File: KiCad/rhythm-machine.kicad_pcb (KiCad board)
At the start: 4 copper layers, 76.2 x 69.8 mm, 23 parts, among them J1 MicroSDModule, J10 Fader, J11 LCD_I2C, J2 AudioAmpModule, J3 Button_LeftRed, J4 Button_LeftGreen, J5 Button_LeftBlue, J6 Button_RightRed, J7 Button_RightGreen, J8 Button_RightBlue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

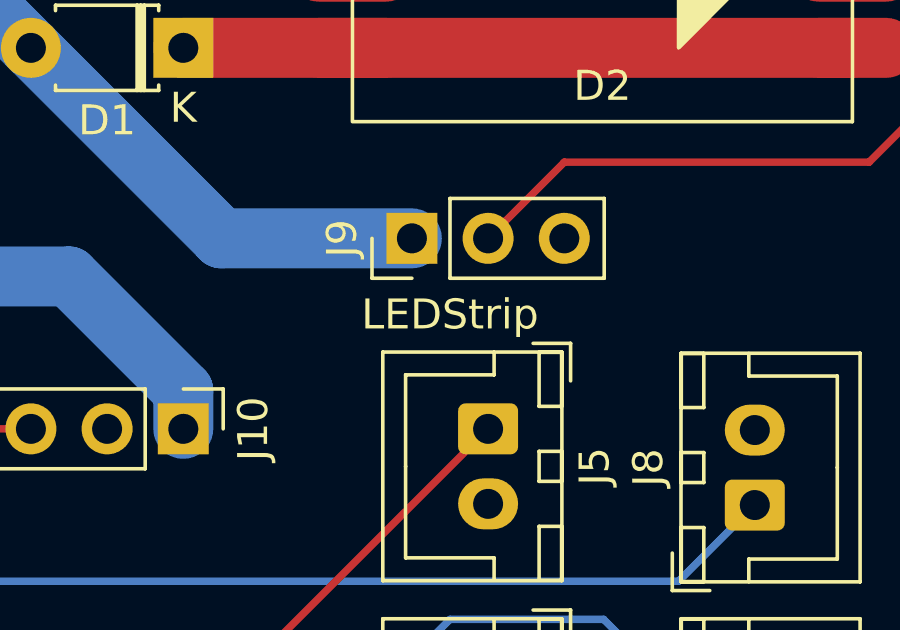
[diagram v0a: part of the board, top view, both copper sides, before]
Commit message: Connected Pico to GND net
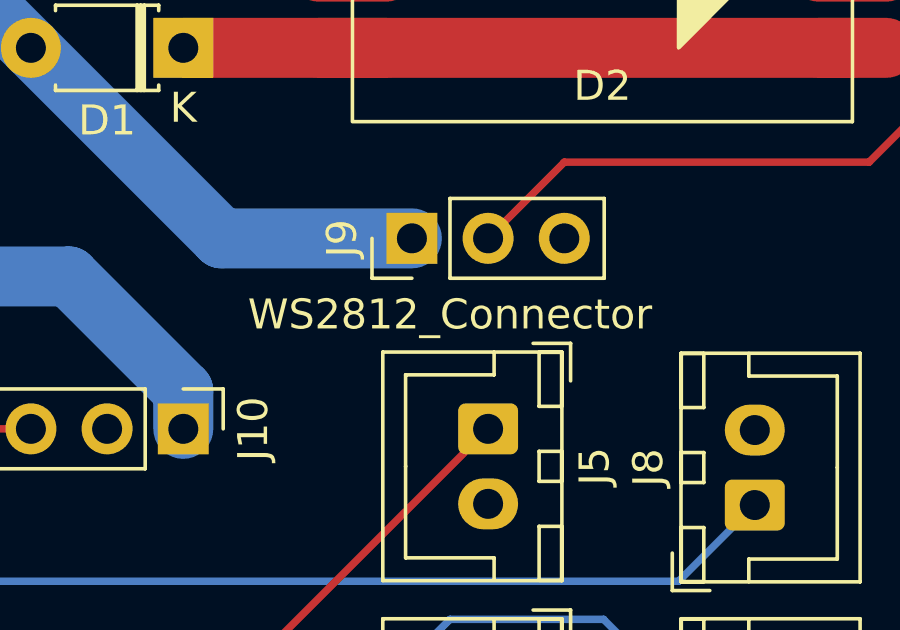
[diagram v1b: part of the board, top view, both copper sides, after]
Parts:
- J9: value LEDStrip -> WS2812_Connector
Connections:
- U1 pad 13: unconnected-(U1-Pad13) -> GND
- U1 pad 18: unconnected-(U1-Pad18) -> GND
- U1 pad 23: unconnected-(U1-Pad23) -> GND
- U1 pad 28: unconnected-(U1-Pad28) -> GND
- U1 pad 3: unconnected-(U1-Pad3) -> GND
- U1 pad 38: unconnected-(U1-Pad38) -> GND
- U1 pad 8: unconnected-(U1-Pad8) -> GND
